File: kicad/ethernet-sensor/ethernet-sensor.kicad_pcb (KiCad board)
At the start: 2 copper layers, 76.2 x 67.3 mm, 20 parts, among them J1 Barrel_Jack, J2 Conn_01x06_Female, J3 Conn_02x05_Top_Bottom, J4 AVR-ISP-10, Q1 BSS138, Q2 BSS138, U1 NCP1117-3.3_SOT223, U2 ATmega328P-PU, Y1 16MHz

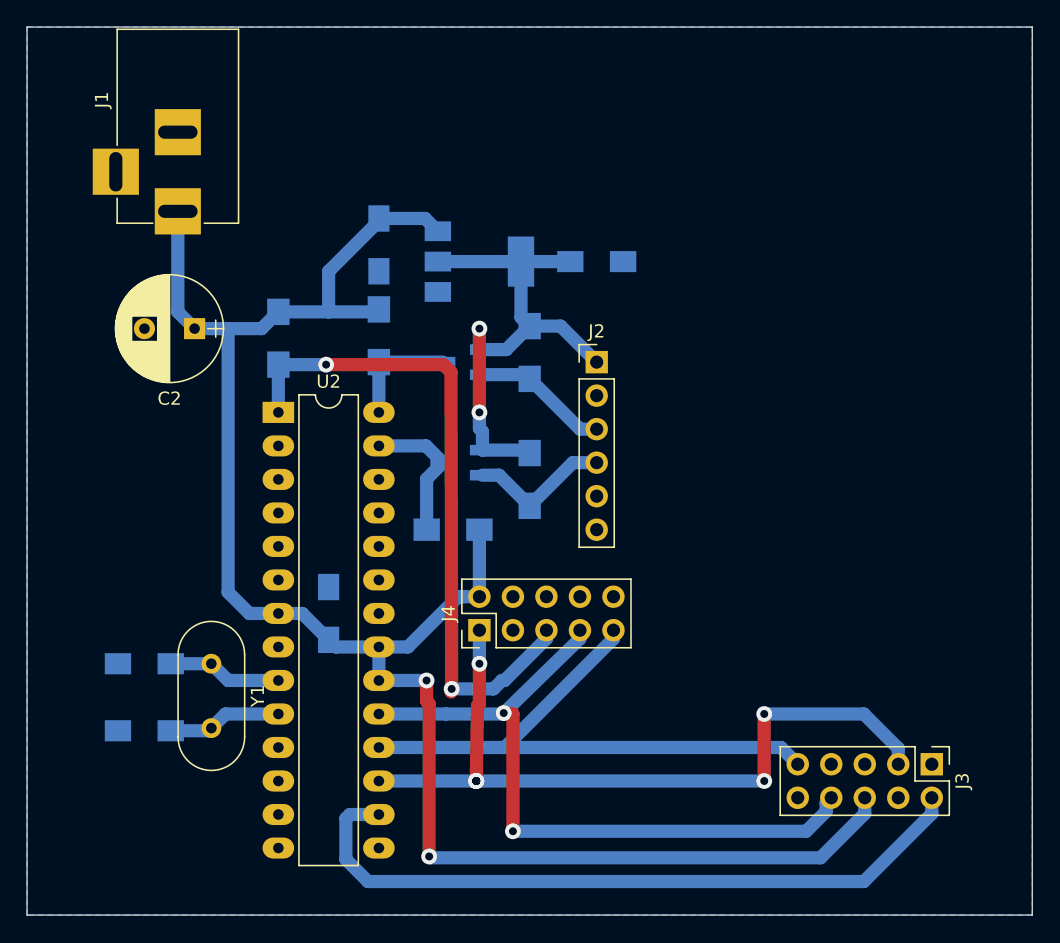
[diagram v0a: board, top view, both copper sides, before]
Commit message: Fix bugs in KiCAD EDA's files
Signed-off-by: Roman Ondráček <ondracek.roman@centrum.cz>
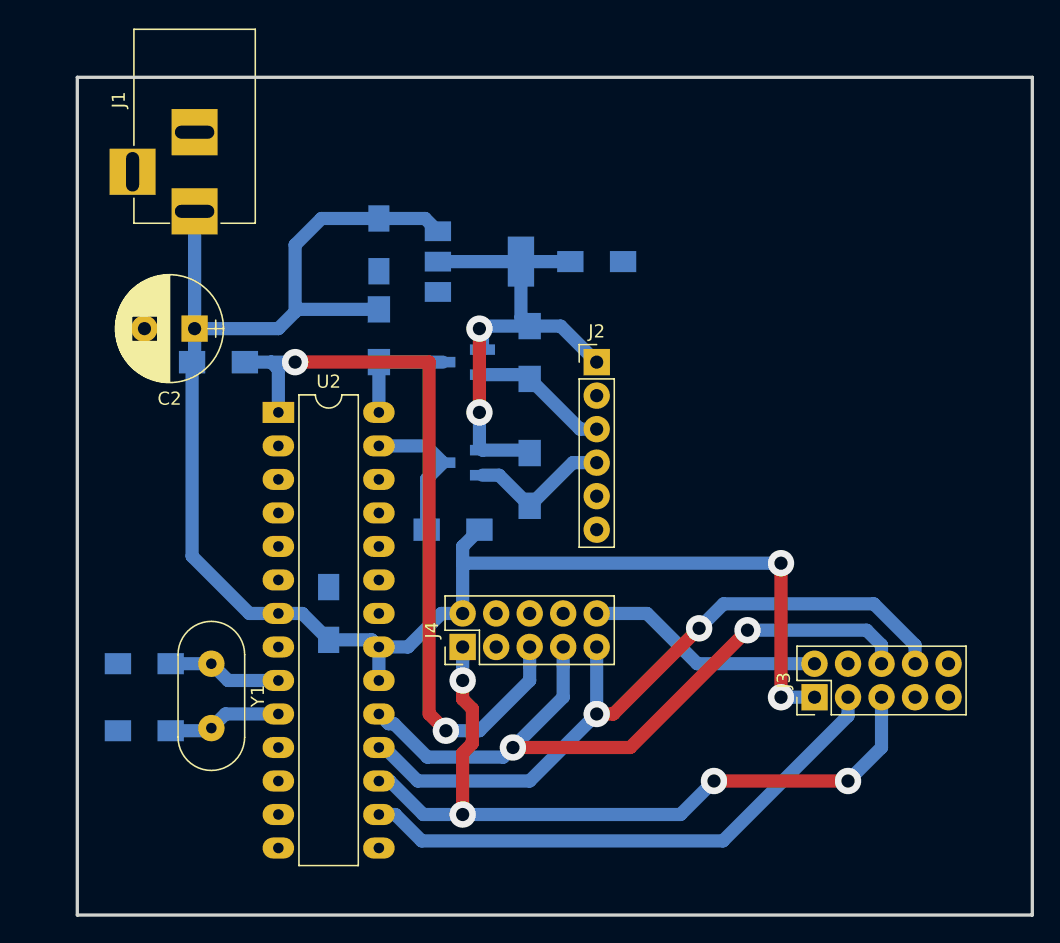
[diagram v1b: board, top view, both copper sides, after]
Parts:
- J2: value Conn_01x06_Female -> Conn_BME280
- J3: value Conn_02x05_Top_Bottom -> Conn_W5100
- moved J3 10.2 mm to (250.2, 100.3), turned to 90 degrees
- moved R5 4.89 mm to (205.0, 74.9), turned to 180 degrees
- moved J4 1.80 mm to (223.5, 96.5)
- moved J1 1.27 mm to (203.2, 63.5)
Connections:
- J3 pad 1: GND -> +5V
- J3 pad 2: SS -> GND
- J3 pad 3: MOSI -> SS
- J3 pad 5: Net-(J3-Pad5) -> MOSI
- J3 pad 6: +5V -> SCK
- J3 pad 8: SCK -> MISO
- J3 pad 9: MISO -> Net-(J3-Pad9)
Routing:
- net GND: track 0.00 -> 18.1 mm
- net SS: track 54.2 -> 41.7 mm
- net +5V: track 140.2 -> 128.9 mm
- net MISO: track 44.1 -> 55.0 mm, vias 0 -> 2
- net RESET: track 50.1 -> 56.9 mm
- net SCK: track 53.0 -> 54.5 mm
- net MOSI: track 58.3 -> 58.9 mm, vias 6 -> 4
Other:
- board size 76.2 x 67.3 mm -> 72.4 x 63.5 mm
- net class Default: clearance 0.8 -> 0.5; via_dia 1.2 -> 2; via_drill 0.6 -> 1
- rule trace_clearance: 0.8 -> 0.5
